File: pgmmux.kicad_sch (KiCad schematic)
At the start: 3 parts

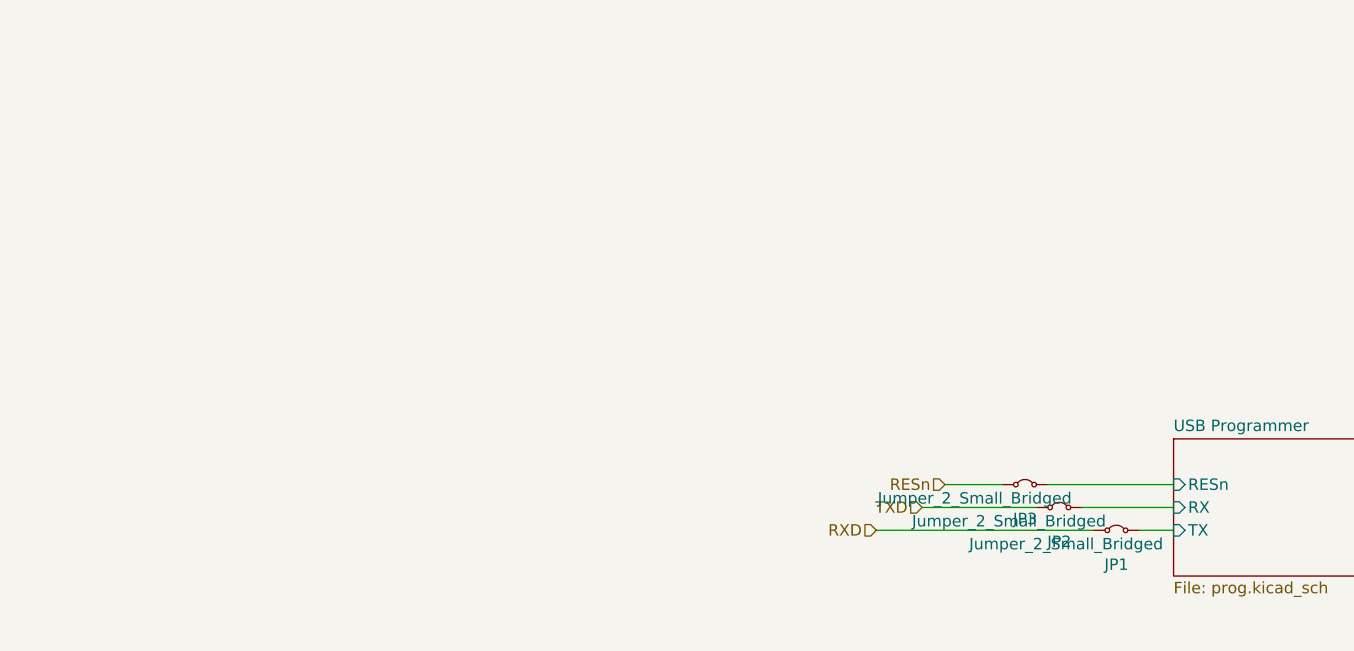
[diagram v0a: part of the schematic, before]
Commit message: pgmmux, sym: TS3A44159PWR symbol
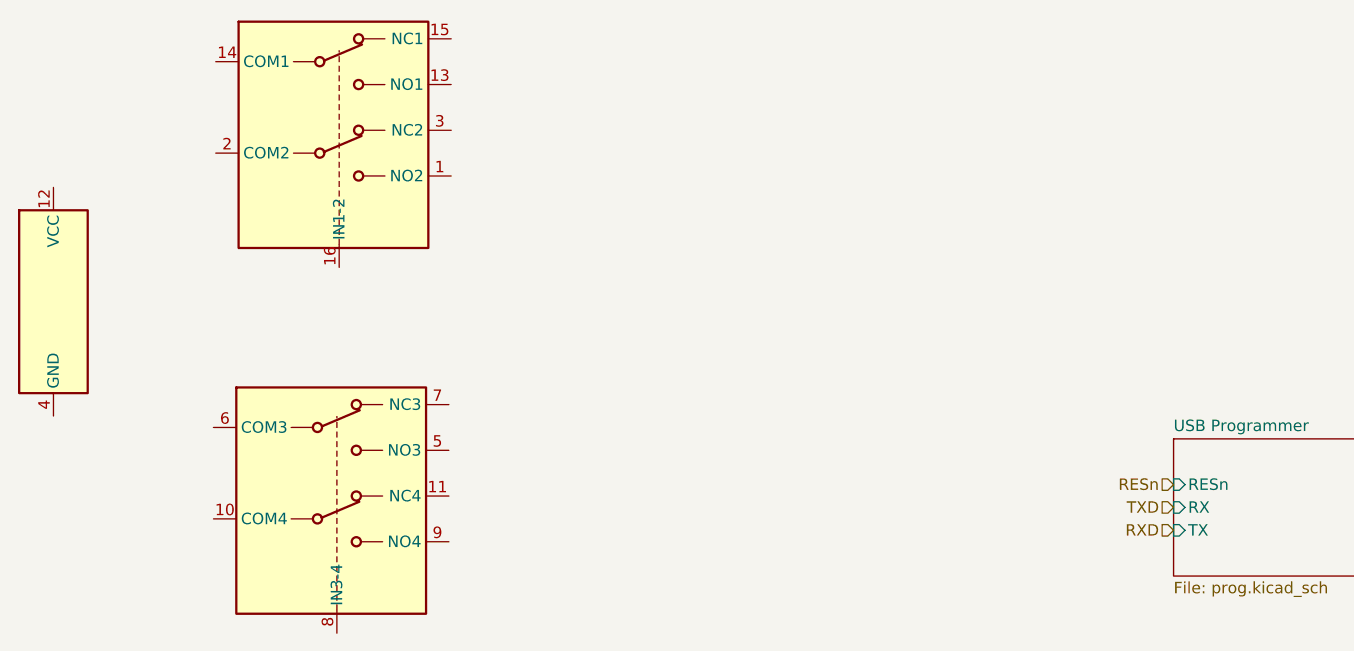
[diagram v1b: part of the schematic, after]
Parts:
- removed JP1, JP2, JP3: Jumper_2_Small_Bridged, Jumper:SolderJumper-2_P1.3mm_Bridged_RoundedPad1.0x1.5mm, symbol Jumper:Jumper_2_Small_Bridged
- added U10: TS3A44159PWR, Package_SO:TSSOP-16_4.4x5mm_P0.65mm, symbol Analog_Switch_Local:TS3A44159PWR

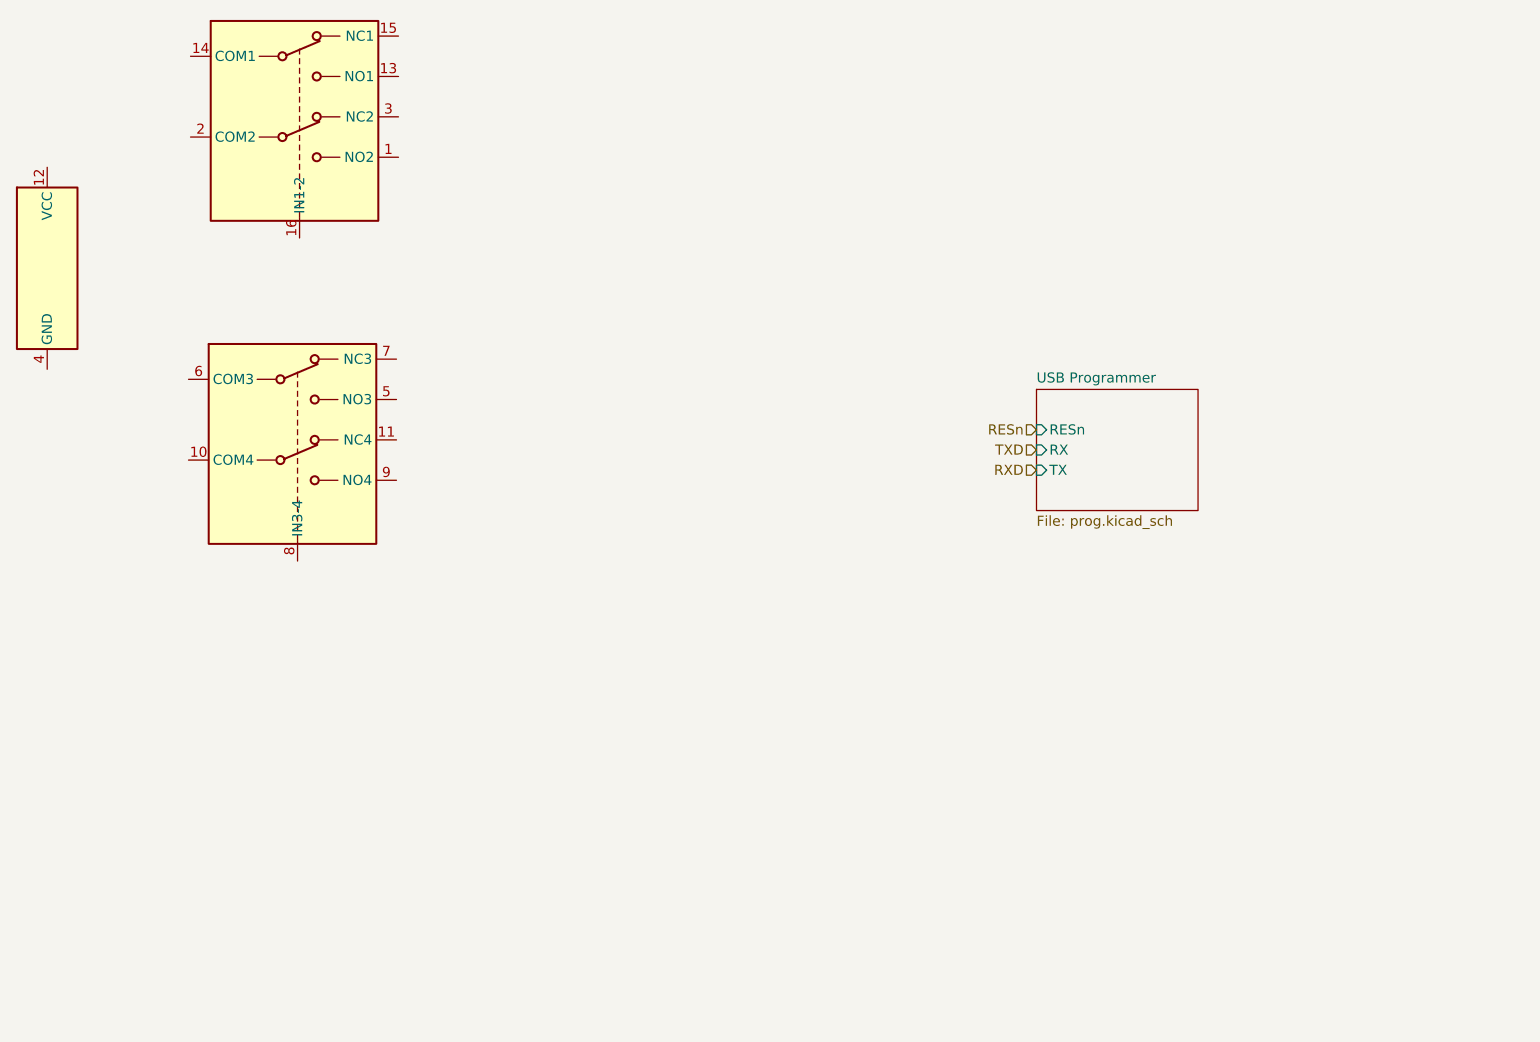
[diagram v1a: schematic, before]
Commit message: pgmmux, pcb: add selector switch
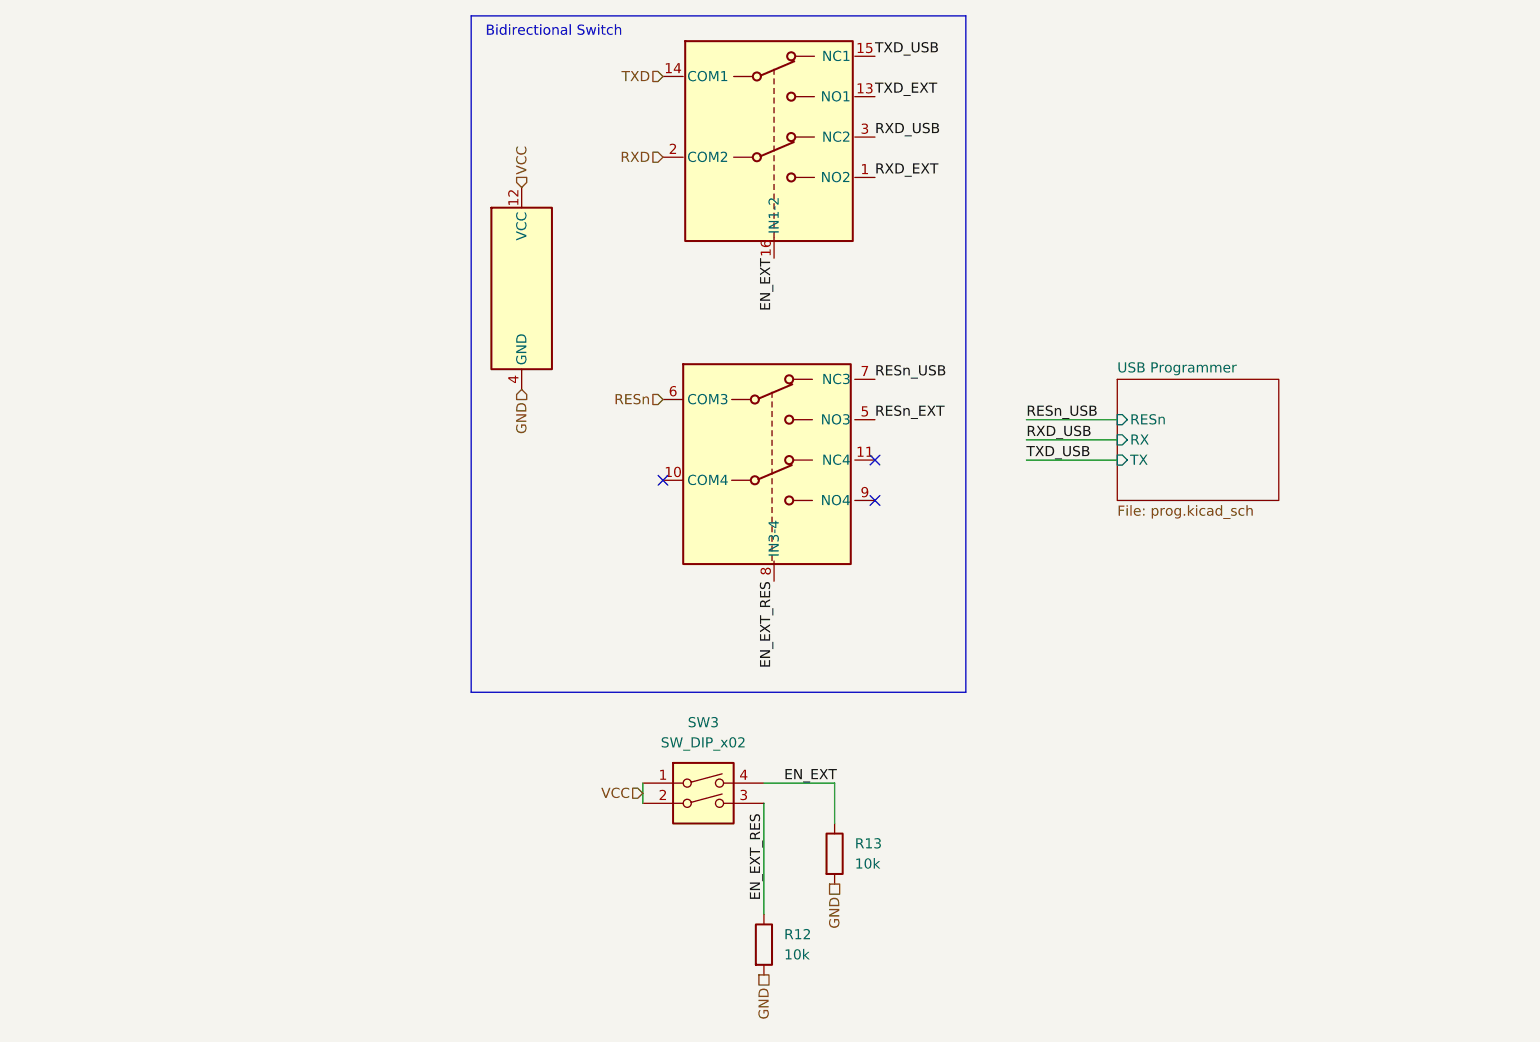
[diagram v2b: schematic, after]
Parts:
- added R12, R13: 10k, Resistor_SMD:R_0402_1005Metric, symbol Device:R
- added SW3: SW_DIP_x02, Button_Switch_SMD:SW_DIP_SPSTx02_Slide_Copal_CHS-02A_W5.08mm_P1.27mm_JPin, symbol Switch:SW_DIP_x02
- U10: Part Number (none) -> TS3A44159PWR
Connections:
- net RESn: now also U10.6 (COM3)
- net RXD: now also U10.2 (COM2)
- net TXD: now also U10.14 (COM1)
- net RESn_EXT: now reaches U10.5 (NO3)
- net RESn_USB: now reaches U10.7 (NC3)
- net EN_EXT_RES: now reaches U10.8 (IN3-4)
- net EN_EXT_RES: now also R12.1, SW3.3
- net VCC: now reaches U10.12 (VCC)
- net VCC: now also SW3.1, SW3.2
- net GND: now reaches U10.4 (GND)
- net GND: now also R12.2, R13.2
- net RXD_EXT: now reaches U10.1 (NO2)
- net TXD_EXT: now reaches U10.13 (NO1)
- net TXD_USB: now reaches U10.15 (NC1)
- net EN_EXT: now reaches U10.16 (IN1-2)
- net EN_EXT: now also R13.1, SW3.4
- net RXD_USB: now reaches U10.3 (NC2)
- no-connect marks 0 -> 3
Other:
- note added: "Bidirectional Switch"

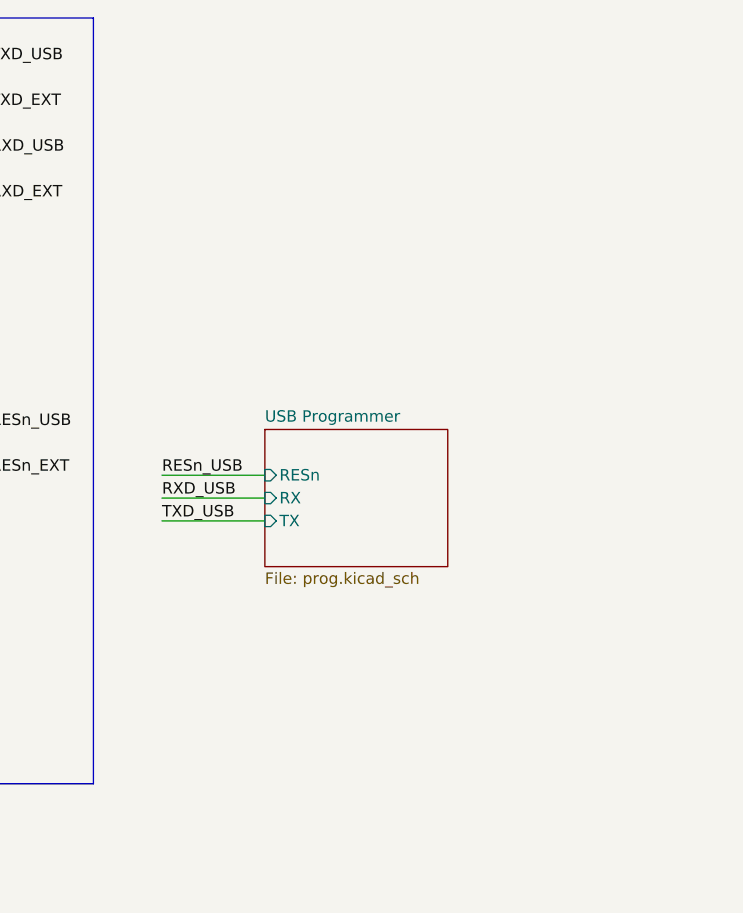
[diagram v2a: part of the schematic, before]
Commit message: pgmmux, pcb:  ext connectors
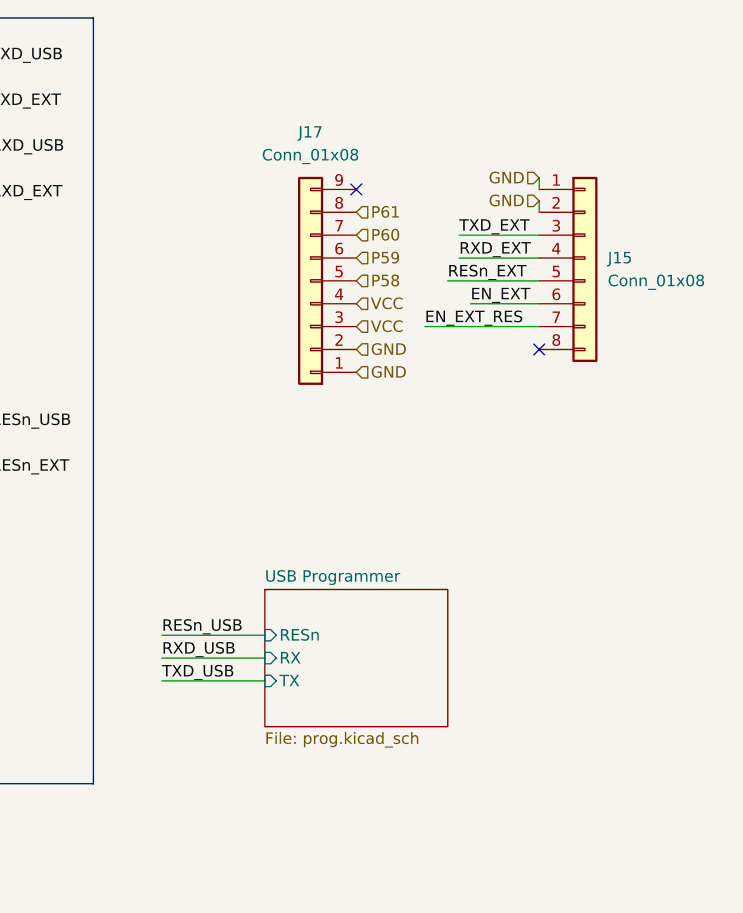
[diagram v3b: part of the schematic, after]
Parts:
- added J15: Conn_01x08, Connector_PinSocket_2.00mm:PinSocket_1x08_P2.00mm_Vertical, symbol Connector_Generic:Conn_01x08
- added J17: Conn_01x08, Connector_PinSocket_2.00mm:PinSocket_1x09_P2.00mm_Vertical, symbol Connector_Generic:Conn_01x09
- SW3: Part Number (none) -> CHS-02TA
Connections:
- net EN_EXT: now also J15.6 (Pin_6)
- net EN_EXT_RES: now also J15.7 (Pin_7)
- net GND: now also J15.1 (Pin_1), J15.2 (Pin_2), J17.1 (Pin_1), J17.2 (Pin_2)
- net RESn_EXT: now also J15.5 (Pin_5)
- net RXD_EXT: now also J15.4 (Pin_4)
- net TXD_EXT: now also J15.3 (Pin_3)
- net VCC: now also J17.3 (Pin_3), J17.4 (Pin_4)
- new net P58: J17.5 (Pin_5)
- new net P59: J17.6 (Pin_6)
- new net P60: J17.7 (Pin_7)
- new net P61: J17.8 (Pin_8)
- no-connect marks 3 -> 5

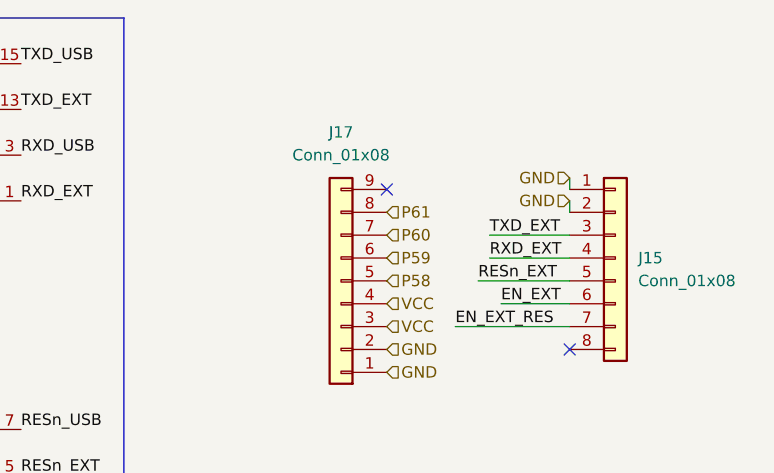
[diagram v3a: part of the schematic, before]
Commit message: docs: add ibom, pcb, psu: fuse, pgmmux, pcb: 2.00mm headers -> 2.54
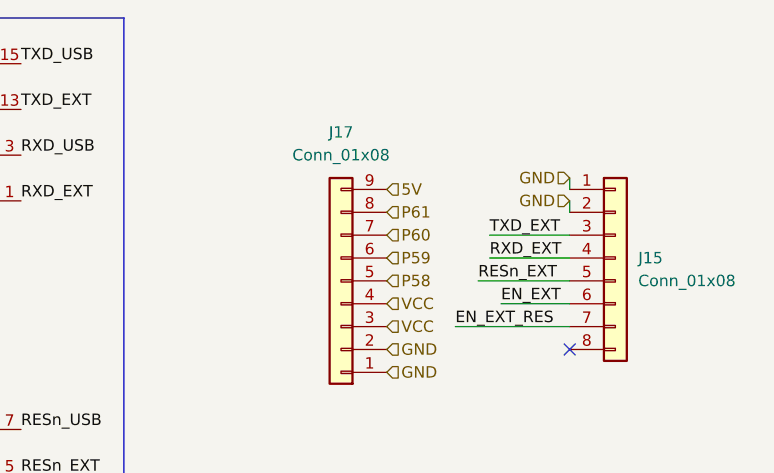
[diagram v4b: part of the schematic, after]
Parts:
- J15: footprint Connector_PinSocket_2.00mm:PinSocket_1x08_P2.00mm_Vertical -> Connector_PinSocket_2.54mm:PinSocket_1x08_P2.54mm_Vertical
- J17: footprint Connector_PinSocket_2.00mm:PinSocket_1x09_P2.00mm_Vertical -> Connector_PinSocket_2.54mm:PinSocket_1x09_P2.54mm_Vertical
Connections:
- net 5V: now reaches J17.9 (Pin_9)
- no-connect marks 5 -> 4
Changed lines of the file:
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@@
-	)
-	(no_connect
-		(at 189.23 59.69)
 	)
 	(no_connect
@@
 		(shape input)
 		(at 189.23 72.39 0)
+		(effects
+			(font
+				(size 1.27 1.27)
+			)
+			(justify left)
+		)
+	)
+	(hierarchical_label "5V"
+		(shape input)
+		(at 189.23 59.69 0)
 		(effects
 			(font
@@
 			)
 		)
-		(property "Footprint" "Connector_PinSocket_2.00mm:PinSocket_1x08_P2.00mm_Vertical"
+		(property "Footprint" "Connector_PinSocket_2.54mm:PinSocket_1x08_P2.54mm_Vertical"
 			(at 214.63 67.31 0)
 			(effects
@@
 			)
 		)
-		(property "Footprint" "Connector_PinSocket_2.00mm:PinSocket_1x09_P2.00mm_Vertical"
+		(property "Footprint" "Connector_PinSocket_2.54mm:PinSocket_1x09_P2.54mm_Vertical"
 			(at 184.15 69.85 0)
 			(effects

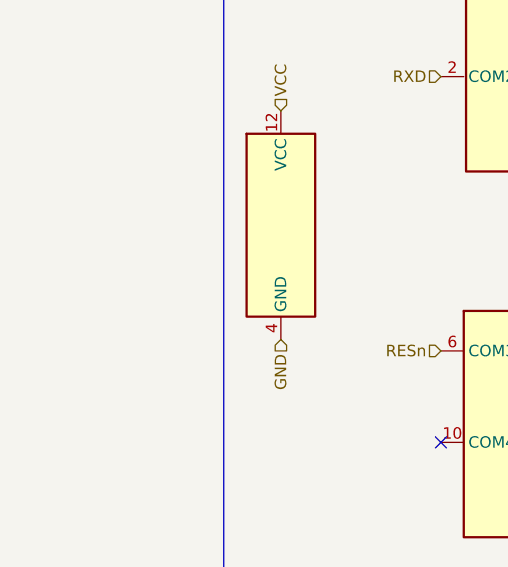
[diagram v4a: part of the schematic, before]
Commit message: pgmmux, pcb: mux bypass cap
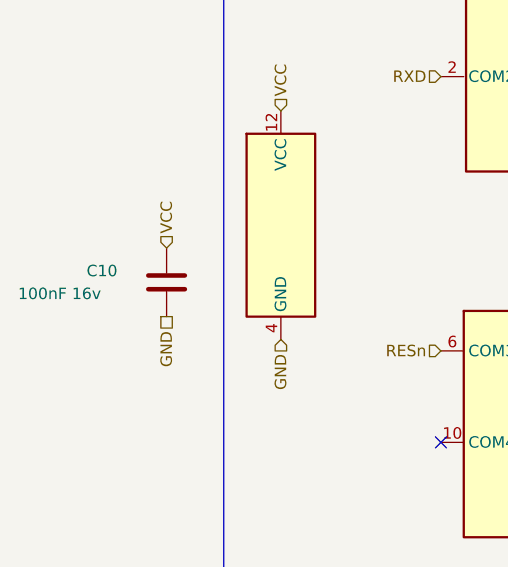
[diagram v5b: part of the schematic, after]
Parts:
- added C10: 100nF 16v, Capacitor_SMD:C_0402_1005Metric, symbol Device:C
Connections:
- net GND: now also C10.1
- net VCC: now also C10.2
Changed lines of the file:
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@@
+		)
+	)
+	(hierarchical_label "GND"
+		(shape passive)
+		(at 91.44 85.09 270)
+		(effects
+			(font
+				(size 1.27 1.27)
+			)
+			(justify right)
+		)
+	)
+	(hierarchical_label "VCC"
+		(shape input)
+		(at 91.44 77.47 90)
+		(effects
+			(font
+				(size 1.27 1.27)
+			)
+			(justify left)
 		)
 	)
@@
 					(unit 1)
 				)
+			)
+		)
+	)
+	(symbol
+		(lib_id "Device:C")
+		(at 91.44 81.28 180)
+		(unit 1)
+		(exclude_from_sim no)
+		(in_bom yes)
+		(on_board yes)
+		(dnp no)
+		(property "Reference" "C10"
+			(at 82.55 80.01 0)
+			(effects
+				(font
+					(size 1.27 1.27)
+				)
+				(justify right)
+			)
+		)
+		(property "Value" "100nF 16v"
+			(at 74.93 82.55 0)
+			(effects
+				(font
+					(size 1.27 1.27)
+				)
+				(justify right)
+			)
+		)
+		(property "Footprint" "Capacitor_SMD:C_0402_1005Metric"
+			(at 90.4748 77.47 0)
+			(effects
+				(font
+					(size 1.27 1.27)
+				)
+				(hide yes)
+			)
+		)
+		(property "Datasheet" "~"
+			(at 91.44 81.28 0)
+			(effects
+				(font
+					(size 1.27 1.27)
+				)
+				(hide yes)
+			)
+		)
+		(property "Description" "Unpolarized capacitor"
+			(at 91.44 81.28 0)
+			(effects
+				(font
+					(size 1.27 1.27)
+				)
+				(hide yes)
+			)
+		)
+		(property "Part Number" "GRM155R71C104KA88D"
+			(at 91.44 81.28 0)
+			(effects
+				(font
+					(size 1.27 1.27)
+				)
+				(hide yes)
+			)
+		)
+		(pin "2"
+		)
+		(pin "1"
+		)
+		(instances
+			(project "P2 Kevinbot Board"
+				(path "/362ca48c-0b77-4943-b8b3-fc15ab97f30d/36ef8cf2-6197-4fa1-9b06-a24478d77804"
+					(reference "C10")
+					(unit 1)
+				)

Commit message: sch, pcb: add part numbers
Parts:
- J15: Part Number (none) -> PPTC081LFBN-RC
- J17: Part Number (none) -> PPTC091LFBN-RC
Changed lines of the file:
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@@
+			)
+		)
+		(property "Part Number" "PPTC081LFBN-RC"
+			(at 214.63 67.31 0)
+			(effects
+				(font
+					(size 1.27 1.27)
+				)
+				(hide yes)
 			)
 		)
@@
 			(at 184.15 69.85 0)
 			(effects
+				(font
+					(size 1.27 1.27)
+				)
+				(hide yes)
+			)
+		)
+		(property "Part Number" "PPTC091LFBN-RC"
+			(at 184.15 69.85 0)
+			(effects
